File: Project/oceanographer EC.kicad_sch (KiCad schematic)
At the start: 32 parts, among them SW1 BOOT0, SW2 RotaryEncoder_Switch, U1 STM32F401CBUx, U2 XC6206PxxxMR, Y1 8 MHz

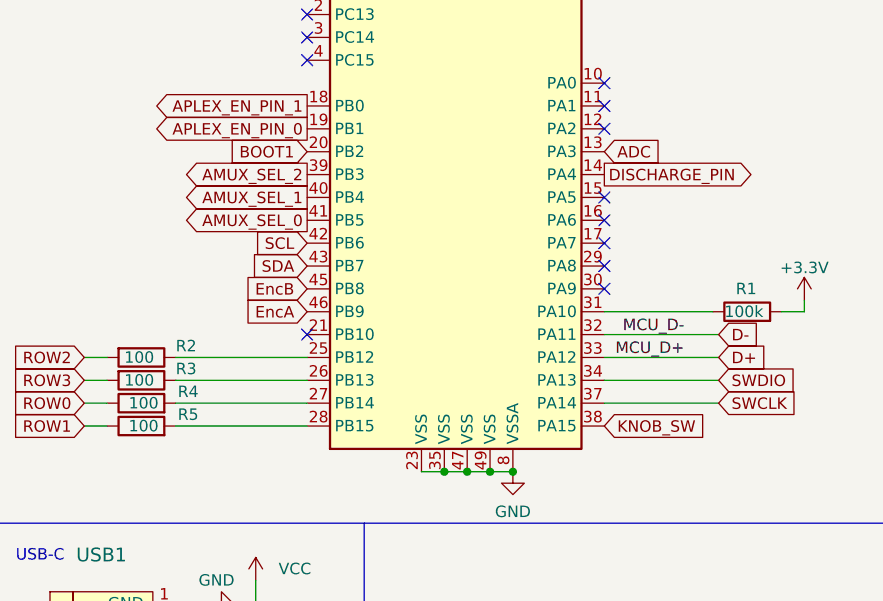
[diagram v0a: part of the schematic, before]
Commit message: redesign after missing switch
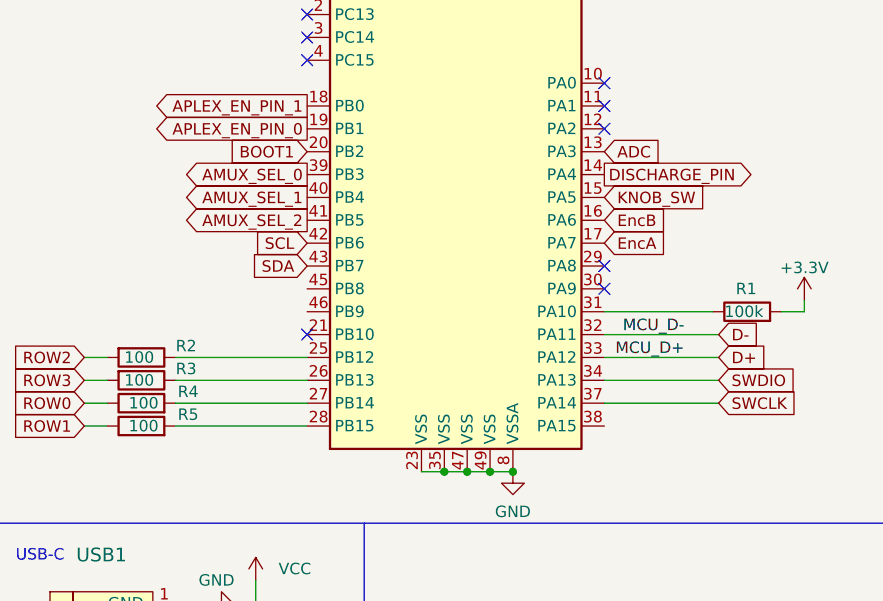
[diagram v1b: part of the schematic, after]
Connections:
- net AMUX_SEL_0: now also U1.39 (PB3); no longer U1.41 (PB5)
- net AMUX_SEL_2: now also U1.41 (PB5); no longer U1.39 (PB3)
- net EncA: now also U1.17 (PA7); no longer U1.46 (PB9)
- net EncB: now also U1.16 (PA6); no longer U1.45 (PB8)
- net KNOB_SW: now also U1.15 (PA5); no longer U1.38 (PA15)
- no-connect marks 14 -> 11
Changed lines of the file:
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@@
   (no_connect (at 46.355 52.705))
   (no_connect (at 79.375 80.645))
-  (no_connect (at 79.375 70.485))
   (no_connect (at 31.75 135.89))
   (no_connect (at 79.375 57.785))
   (no_connect (at 79.375 62.865))
   (no_connect (at 31.75 120.65))
-  (no_connect (at 79.375 73.025))
   (no_connect (at 79.375 78.105))
   (no_connect (at 79.375 60.325))
-  (no_connect (at 79.375 75.565))
   (no_connect (at 46.355 85.725))
   (no_connect (at 46.355 50.165))
@@
     )
   )
-  (global_label "EncA" (shape input) (at 46.355 83.185 180)
-    (effects (font (size 1.27 1.27)) (justify right))
-    (property "Intersheetrefs" "${INTERSHEET_REFS}" (at 46.355 83.185 0)
-      (effects (font (size 1.27 1.27)) hide)
+  (global_label "EncA" (shape input) (at 79.375 75.565 0)
+    (effects (font (size 1.27 1.27)) (justify left))
+    (property "Intersheetrefs" "${INTERSHEET_REFS}" (at 79.375 75.565 0)
+      (effects (font (size 1.27 1.27)) (justify left) hide)
     )
   )
@@
     )
   )
-  (global_label "AMUX_SEL_2" (shape output) (at 46.355 67.945 180) (fields_autoplaced)
-    (effects (font (size 1.27 1.27)) (justify right))
-    (property "Intersheetrefs" "${INTERSHEET_REFS}" (at 32.3305 67.8656 0)
+  (global_label "AMUX_SEL_2" (shape output) (at 46.355 73.025 180) (fields_autoplaced)
+    (effects (font (size 1.27 1.27)) (justify right))
+    (property "Intersheetrefs" "${INTERSHEET_REFS}" (at 32.3305 72.9456 0)
       (effects (font (size 1.27 1.27)) (justify right) hide)
     )
@@
     )
   )
-  (global_label "KNOB_SW" (shape input) (at 79.375 95.885 0) (fields_autoplaced)
-    (effects (font (size 1.27 1.27)) (justify left))
-    (property "Intersheetrefs" "${INTERSHEET_REFS}" (at 91.1103 95.885 0)
+  (global_label "KNOB_SW" (shape input) (at 79.375 70.485 0) (fields_autoplaced)
+    (effects (font (size 1.27 1.27)) (justify left))
+    (property "Intersheetrefs" "${INTERSHEET_REFS}" (at 91.1103 70.485 0)
       (effects (font (size 1.27 1.27)) (justify left) hide)
     )
@@
     )
   )
-  (global_label "AMUX_SEL_0" (shape output) (at 46.355 73.025 180) (fields_autoplaced)
-    (effects (font (size 1.27 1.27)) (justify right))
-    (property "Intersheetrefs" "${INTERSHEET_REFS}" (at 32.3305 73.1044 0)
+  (global_label "AMUX_SEL_0" (shape output) (at 46.355 67.945 180) (fields_autoplaced)
+    (effects (font (size 1.27 1.27)) (justify right))
+    (property "Intersheetrefs" "${INTERSHEET_REFS}" (at 32.3305 68.0244 0)
       (effects (font (size 1.27 1.27)) (justify right) hide)
     )
@@
     )
   )
-  (global_label "EncB" (shape input) (at 46.355 80.645 180)
-    (effects (font (size 1.27 1.27)) (justify right))
-    (property "Intersheetrefs" "${INTERSHEET_REFS}" (at 46.355 80.645 0)
-      (effects (font (size 1.27 1.27)) hide)
-    )
-  )
+  (global_label "EncB" (shape input) (at 79.375 73.025 0)
+    (effects (font (size 1.27 1.27)) (justify left))
+    (property "Intersheetrefs" "${INTERSHEET_REFS}" (at 79.375 73.025 0)
+      (effects (font (size 1.27 1.27)) (justify left) hide)
+    )
+  )

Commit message: fresh gerbers
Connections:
- no-connect marks 11 -> 14
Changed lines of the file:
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@@
   (junction (at 70.485 189.23) (diameter 0) (color 0 0 0 0)
   )
+  (no_connect (at 79.375 95.885))
   (no_connect (at 46.355 52.705))
   (no_connect (at 79.375 80.645))
+  (no_connect (at 46.355 80.645))
   (no_connect (at 31.75 135.89))
   (no_connect (at 79.375 57.785))
@@
   (no_connect (at 46.355 85.725))
   (no_connect (at 46.355 50.165))
+  (no_connect (at 46.355 83.185))
   (no_connect (at 46.355 55.245))
   (wire (pts (xy 102.87 191.135) (xy 102.87 184.785))
